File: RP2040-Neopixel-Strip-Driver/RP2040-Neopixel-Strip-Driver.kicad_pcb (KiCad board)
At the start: 4 copper layers, 20.3 x 48.3 mm, 45 parts, among them J201 TYPE-C-31-M-12, J202 Conn_01x03, J203 NeopixelStrip, SW202 ~{USB_BOOT}, U201 AZ1117R-3.3TRE1, U202 RP2040, U205 W25Q128JVS, Y201 Crystal_GND24

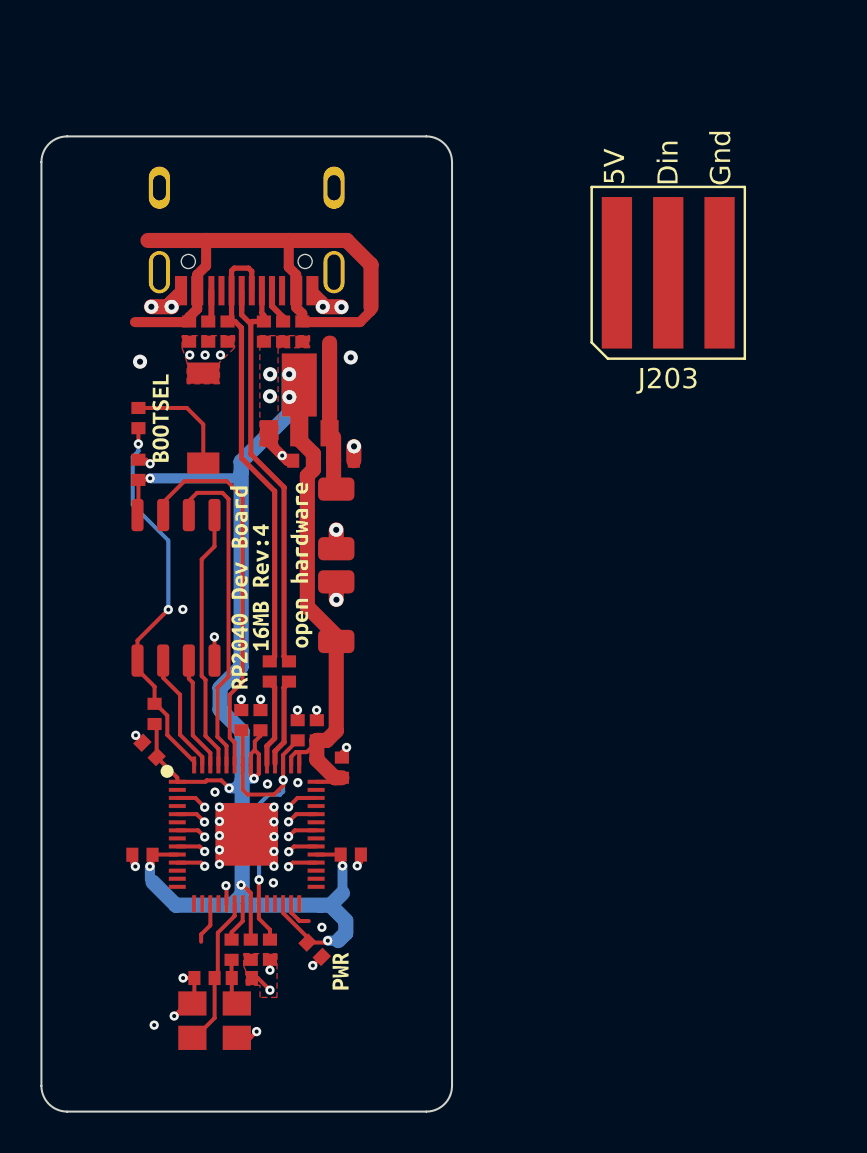
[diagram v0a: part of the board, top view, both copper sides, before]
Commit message: Made new LED strip model and narrowed board.
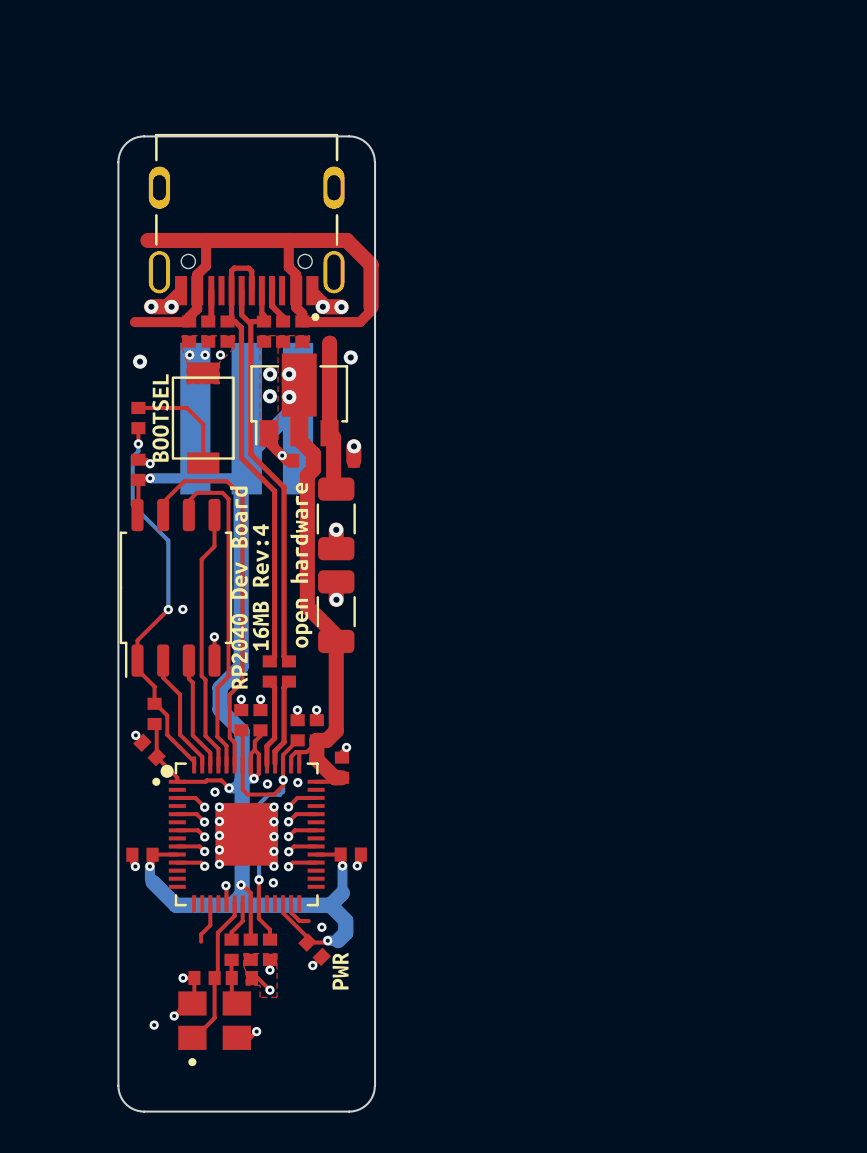
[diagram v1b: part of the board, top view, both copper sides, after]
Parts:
- J203: moved to B.Cu
- moved kibuzzard-62659E4E 59.4 mm to (212.5, 48.8)
- moved kibuzzard-62659F2B 59.4 mm to (200.1, 36.4)
- moved kibuzzard-6265A538 59.4 mm to (206.1, 35.8)
- moved J203 22.1 mm to (146.9, 40.7), turned to 180 degrees
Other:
- board size 20.3 x 48.3 mm -> 12.7 x 48.3 mm

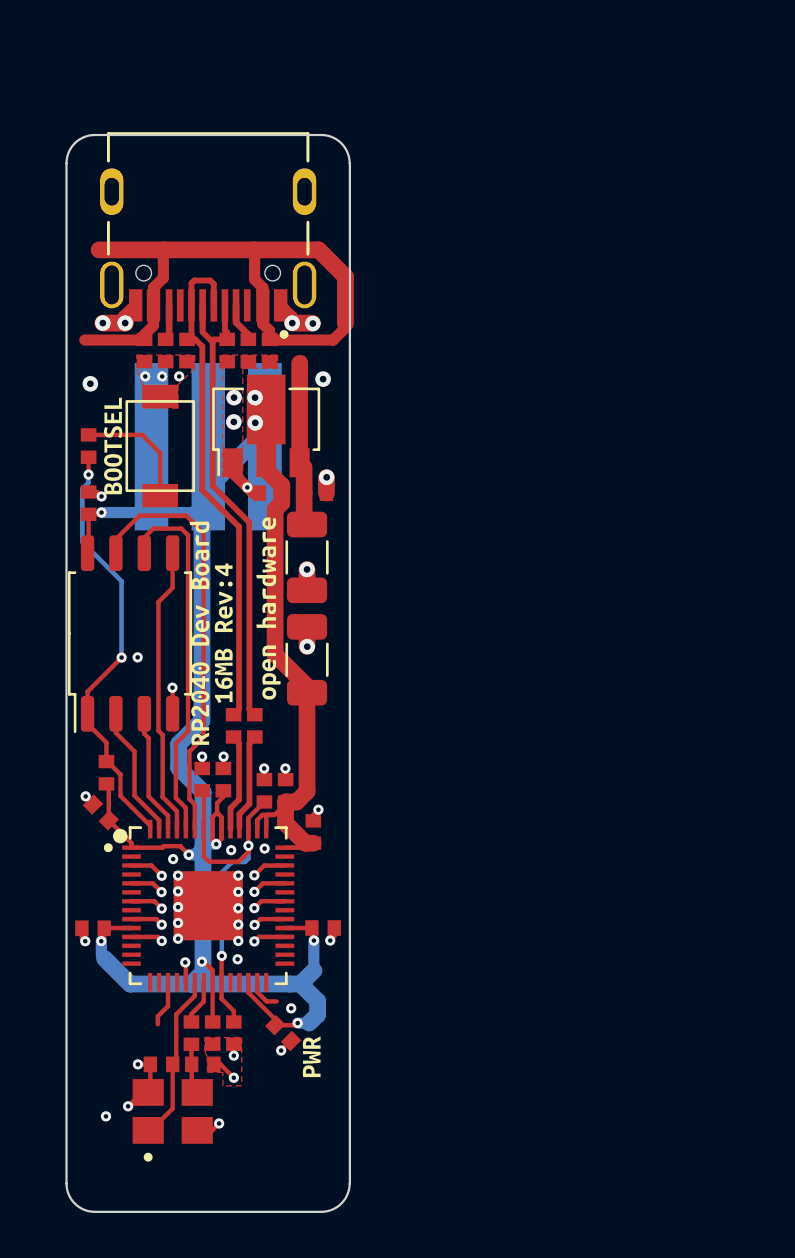
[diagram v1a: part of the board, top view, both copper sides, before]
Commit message: Continued to shrink PCB, replaced regulator and mem with smaller ICs, removed 1206 caps
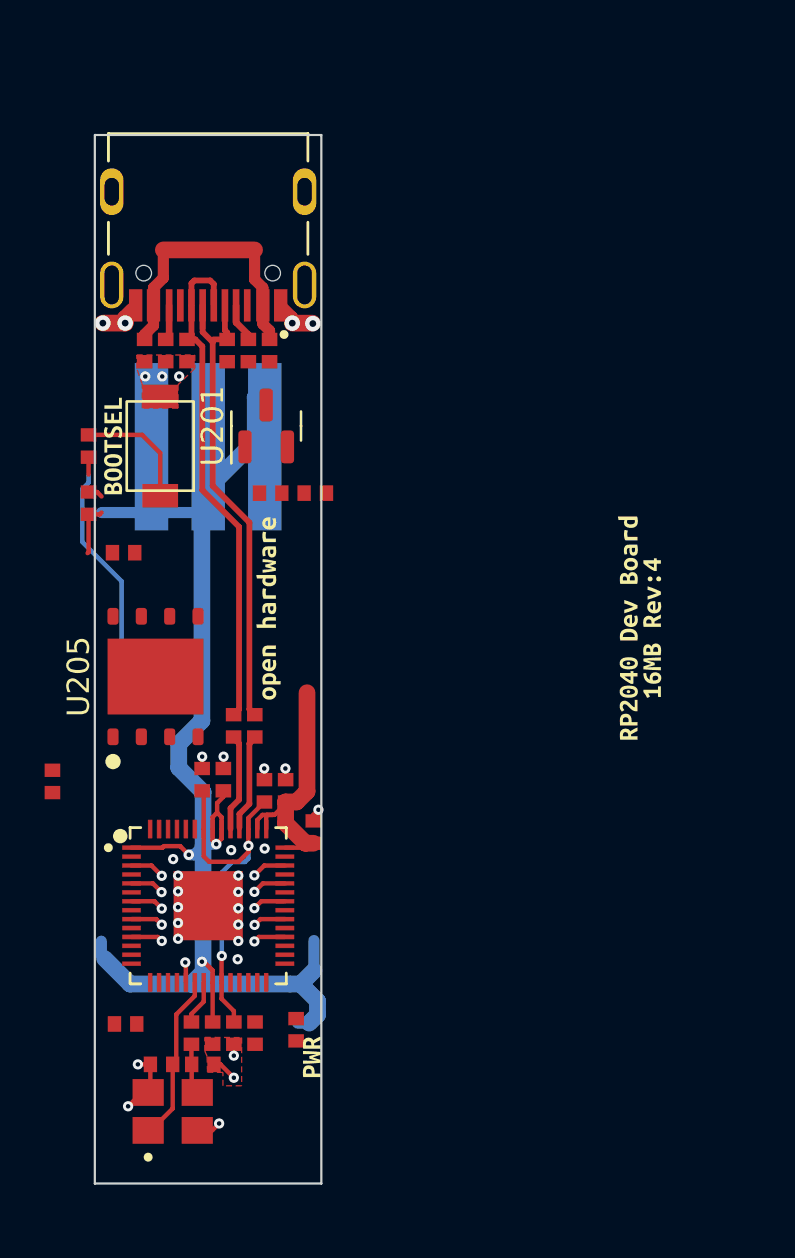
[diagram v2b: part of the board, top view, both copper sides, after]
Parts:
- removed C209, C210: 100uF, Capacitor_SMD:C_1206_3216Metric
- U201: value AZ1117R-3.3TRE1 -> XC6206P332MR; footprint Package_TO_SOT_SMD:SOT-89-3 -> Package_TO_SOT_SMD:SOT-23
- U205: value W25Q128JVS -> W25Q128JVPIQ; footprint Package_SO:SOIC-8_5.23x5.23mm_P1.27mm -> Package_SON:WSON-8-1EP_6x5mm_P1.27mm_EP3.4x4.3mm
- moved kibuzzard-628425F6 19.2 mm to (165.7, 48.9)
- moved kibuzzard-62842605 19.2 mm to (166.8, 48.9)
- moved R213 9.89 mm to (143.1, 45.5), turned to -90 degrees
- moved C213 4.72 mm to (150.8, 66.9), turned to 180 degrees
- moved C215 4.53 mm to (143.2, 66.6), turned to -90 degrees
- moved C212 2.58 mm to (139.9, 55.7), turned to 0 degrees
- moved U205 2.24 mm to (144.6, 51.0)
- moved C221 1.26 mm to (149.0, 67.0), turned to 180 degrees
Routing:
- net 3V3_LDO: track 97.9 -> 74.2 mm, vias 9 -> 3
- net /RP2040/MCU_QSPI_SD3: track 18.9 -> 0.00 mm
- net /RP2040/MCU_QSPI_SCLK: track 16.5 -> 0.00 mm
- net VBUS: track 28.8 -> 12.8 mm
- net /RP2040/MCU_QSPI_SD0: track 13.0 -> 0.00 mm
- net /RP2040/MCU_QSPI_CSN: track 19.3 -> 9.82 mm, vias 2 -> 0
- net GND: track 23.6 -> 14.8 mm, vias 49 -> 32
- net VHI: track 7.50 -> 0.00 mm
- net /RP2040/MCU_QSPI_SD1: track 5.97 -> 0.00 mm
- net /RP2040/MCU_QSPI_SD2: track 5.61 -> 0.00 mm
- net GPIO14: track 2.07 -> 0.00 mm
- net GPIO16: track 1.48 -> 0.00 mm
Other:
- board size 12.7 x 48.3 mm -> 10.2 x 47 mm

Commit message: Update RP2040-Neopixel-Strip-Driver.kicad_pcb
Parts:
- moved kibuzzard-62842635 38.6 mm to (127.6, 37.8)
- moved kibuzzard-62842613 20.0 mm to (169.3, 44.8)
- moved kibuzzard-6284261D 12.9 mm to (130.0, 38.1)
- moved R213 12.0 mm to (131.7, 42.0)
- moved C201 10.5 mm to (162.2, 43.3)
- moved U201 10.3 mm to (150.6, 50.0)
- moved C222 8.27 mm to (134.2, 39.5)
- moved C207 7.37 mm to (157.1, 43.3)
- moved R211 5.42 mm to (136.8, 38.2)
- moved C213 4.11 mm to (151.5, 62.8)
- moved C215 3.90 mm to (142.3, 62.8), turned to 180 degrees
- moved U205 3.10 mm to (144.6, 47.9)
- moved C204 2.64 mm to (151.8, 53.9)
- moved SW202 2.59 mm to (146.9, 39.2), turned to 90 degrees
- moved C208 2.50 mm to (144.9, 53.9)
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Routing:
- net 3V3_LDO: track 74.2 -> 32.4 mm
- net /RP2040/USB_D-: track 22.5 -> 5.05 mm
- net /RP2040/USB_D+: track 22.8 -> 5.49 mm
- net /RP2040/MCU_QSPI_CSN: track 9.82 -> 0.00 mm
- net Net-(R211-Pad1): track 5.46 -> 0.00 mm
- net /RP2040/MCU_USB_D+: track 4.38 -> 0.00 mm
- net /RP2040/MCU_USB_D-: track 4.35 -> 0.00 mm
- net GND: track 14.8 -> 11.4 mm, vias 32 -> 24
- net +1V1: track 16.8 -> 13.5 mm

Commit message: Update RP2040-Neopixel-Strip-Driver.kicad_pcb
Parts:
- moved J203 36.4 mm to (110.6, 38.9)
- moved R211 13.0 mm to (144.4, 48.7), turned to 0 degrees
- moved R213 12.7 mm to (142.7, 48.4), turned to 180 degrees
- moved C212 4.22 mm to (142.3, 59.2), turned to 180 degrees
- moved U205 3.77 mm to (144.6, 44.2)
- moved SW202 1.27 mm to (148.2, 39.2)
- moved C216 1.21 mm to (151.5, 59.2), turned to 180 degrees
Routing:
- net 3V3_LDO: track 32.4 -> 16.4 mm
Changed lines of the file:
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@@
   )
   (footprint "Package_SON:WSON-8-1EP_6x5mm_P1.27mm_EP3.4x4.3mm" (layer "F.Cu")
-    (at 144.565 47.93 90)
+    (at 144.57 44.16 90)
     (descr "WSON, 8 Pin (http://www.winbond.com/resource-files/w25q32jv%20revg%2003272018%20plus.pdf (page 68)), generated with kicad-footprint-generator ipc_noLead_generator.py")
     (tags "WSON NoLead")
@@
   )
   (footprint "Breadstick Footprints:Perfect_0402_Cap" (layer "F.Cu")
-    (at 151.62 58)
+    (at 151.49 59.2 180)
     (property "JLCPCB P/N" "C15525")
     (property "Sheetfile" "RP2040.kicad_sch")
@@
     (fp_line (start -0.85 -1.3) (end 0.85 -1.3) (layer "F.Fab") (width 0.12))
     (fp_line (start -0.85 1.3) (end -0.85 -1.3) (layer "F.Fab") (width 0.12))
-    (pad "1" smd rect (at 0 0.5) (size 0.7 0.6) (layers "F.Cu" "F.Paste" "F.Mask")
+    (pad "1" smd rect (at 0 0.5 180) (size 0.7 0.6) (layers "F.Cu" "F.Paste" "F.Mask")
       (net 53 "3V3_LDO") (pintype "passive"))
-    (pad "2" smd rect (at 0 -0.5) (size 0.7 0.6) (layers "F.Cu" "F.Paste" "F.Mask")
+    (pad "2" smd rect (at 0 -0.5 180) (size 0.7 0.6) (layers "F.Cu" "F.Paste" "F.Mask")
       (net 1 "GND") (pintype "passive"))
     (model "${KICAD6_3DMODEL_DIR}/Capacitor_SMD.3dshapes/C_0402_1005Metric.step"
@@
   )
   (footprint "Breadstick Footprints:Perfect_0402_Resistor" (layer "F.Cu")
-    (at 131.67 42 -90)
+    (at 142.66 48.41 180)
     (property "JLCPCB P/N" "C25744")
     (property "Sheetfile" "RP2040.kicad_sch")
     (property "Sheetname" "RP2040")
     (attr through_hole)
-    (fp_text reference "R213" (at -0.05 1.19) (layer "F.Fab")
+    (fp_text reference "R213" (at -0.05 1.19 90) (layer "F.Fab")
       (effects (font (size 1 1) (thickness 0.15)))
     )
-    (fp_text value "10k" (at 6.8 0.04) (layer "F.Fab")
+    (fp_text value "10k" (at 6.8 0.04 90) (layer "F.Fab")
       (effects (font (size 1 1) (thickness 0.15)))
     )
@@
     (fp_line (start -0.85 -1.3) (end 0.85 -1.3) (layer "F.Fab") (width 0.12))
     (fp_line (start 0.85 -1.3) (end 0.85 1.3) (layer "F.Fab") (width 0.12))
-    (pad "1" smd rect (at 0 0.5 270) (size 0.7 0.6) (layers "F.Cu" "F.Paste" "F.Mask")
+    (pad "1" smd rect (at 0 0.5 180) (size 0.7 0.6) (layers "F.Cu" "F.Paste" "F.Mask")
       (net 16 "/RP2040/MCU_QSPI_CSN") (pintype "passive"))
-    (pad "2" smd rect (at 0 -0.5 270) (size 0.7 0.6) (layers "F.Cu" "F.Paste" "F.Mask")
+    (pad "2" smd rect (at 0 -0.5 180) (size 0.7 0.6) (layers "F.Cu" "F.Paste" "F.Mask")
       (net 53 "3V3_LDO") (pintype "passive"))
     (model "${KICAD6_3DMODEL_DIR}/Resistor_SMD.3dshapes/R_0402_1005Metric.step"
@@
   )
   (footprint "Breadstick Footprints:GT-TC029B-H025-L1N" (layer "F.Cu")
-    (at 146.91 39.25 90)
+    (at 148.175 39.25 90)
     (property "JLCPCB P/N" "C843669")
     (property "Sheetfile" "RP2040.kicad_sch")
@@
   )
   (footprint "Breadstick Footprints:Perfect_0402_Resistor" (layer "F.Cu")
-    (at 136.75 38.19 180)
+    (at 144.44 48.68)
     (property "JLCPCB P/N" "C11702")
     (property "Sheetfile" "RP2040.kicad_sch")
@@
     (fp_line (start -0.85 -1.3) (end 0.85 -1.3) (layer "F.Fab") (width 0.12))
     (fp_line (start 0.85 -1.3) (end 0.85 1.3) (layer "F.Fab") (width 0.12))
-    (pad "1" smd rect (at 0 0.5 180) (size 0.7 0.6) (layers "F.Cu" "F.Paste" "F.Mask")
+    (pad "1" smd rect (at 0 0.5) (size 0.7 0.6) (layers "F.Cu" "F.Paste" "F.Mask")
       (net 15 "Net-(R211-Pad1)") (pintype "passive"))
-    (pad "2" smd rect (at 0 -0.5 180) (size 0.7 0.6) (layers "F.Cu" "F.Paste" "F.Mask")
+    (pad "2" smd rect (at 0 -0.5) (size 0.7 0.6) (layers "F.Cu" "F.Paste" "F.Mask")
       (net 16 "/RP2040/MCU_QSPI_CSN") (pintype "passive"))
     (model "${KICAD6_3DMODEL_DIR}/Resistor_SMD.3dshapes/R_0402_1005Metric.step"
@@
   )
   (footprint "Breadstick Footprints:Perfect_0402_Cap" (layer "F.Cu")
-    (at 139.93 55.73)
+    (at 142.33 59.2 180)
     (property "JLCPCB P/N" "C15525")
     (property "Sheetfile" "RP2040.kicad_sch")
@@
     (fp_line (start -0.85 -1.3) (end 0.85 -1.3) (layer "F.Fab") (width 0.12))
     (fp_line (start -0.85 1.3) (end -0.85 -1.3) (layer "F.Fab") (width 0.12))
-    (pad "1" smd rect (at 0 0.5) (size 0.7 0.6) (layers "F.Cu" "F.Paste" "F.Mask")
+    (pad "1" smd rect (at 0 0.5 180) (size 0.7 0.6) (layers "F.Cu" "F.Paste" "F.Mask")
       (net 53 "3V3_LDO") (pintype "passive"))
-    (pad "2" smd rect (at 0 -0.5) (size 0.7 0.6) (layers "F.Cu" "F.Paste" "F.Mask")
+    (pad "2" smd rect (at 0 -0.5 180) (size 0.7 0.6) (layers "F.Cu" "F.Paste" "F.Mask")
       (net 1 "GND") (pintype "passive"))
     (model "${KICAD6_3DMODEL_DIR}/Capacitor_SMD.3dshapes/C_0402_1005Metric.step"
@@
   )
   (footprint "Breadstick Footprints:NeopixelStrip" (layer "B.Cu")
-    (at 146.91 40.73 180)
+    (at 110.58 38.9 180)
     (property "Sheetfile" "RP2040.kicad_sch")
     (property "Sheetname" "RP2040")
@@
   (segment (start 147.31 56.7) (end 147.31 57.13) (width 0.2) (layer "F.Cu") (net 53))
   (segment (start 146.72 63.81) (end 146.63 63.81) (width 0.2) (layer "F.Cu") (net 53))
-  (segment (start 151.42 58.7) (end 151.62 58.5) (width 0.2) (layer "F.Cu") (net 53))
   (segment (start 147.11 57.865) (end 147.11 57.33) (width 0.2) (layer "F.Cu") (net 53))
   (segment (start 146.99 64.08) (end 146.72 63.81) (width 0.2) (layer "F.Cu") (net 53))
@@
   (via (at 146.63 63.81) (size 0.46) (drill 0.2) (layers "F.Cu" "B.Cu") (net 53))
   (via (at 147.27 58.54) (size 0.46) (drill 0.2) (layers "F.Cu" "B.Cu") (net 53))
-  (segment (start 142.12 62.89) (end 142.12 63.52) (width 0.5) (layer "B.Cu") (net 53))
-  (segment (start 143.41 64.81) (end 142.27 63.67) (width 0.75) (layer "B.Cu") (net 53))
-  (segment (start 150.58 64.81) (end 146.15 64.81) (width 0.75) (layer "B.Cu") (net 53))
-  (segment (start 146.15 64.81) (end 146.68 64.28) (width 0.75) (layer "B.Cu") (net 53))
   (segment (start 147.27 58.54) (end 146.76 58.54) (width 0.5) (layer "B.Cu") (net 53))
-  (segment (start 151.65 64.21) (end 151.05 64.81) (width 0.75) (layer "B.Cu") (net 53))
   (segment (start 146.68 58.62) (end 146.68 61.98) (width 0.75) (layer "B.Cu") (net 53))
-  (segment (start 151.05 64.81) (end 151.81 65.57) (width 0.75) (layer "B.Cu") (net 53))
   (segment (start 146.042396 59.017918) (end 146.282082 59.017918) (width 0.5) (layer "B.Cu") (net 53))
-  (segment (start 151.65 62.86) (end 151.65 64.21) (width 0.5) (layer "B.Cu") (net 53))
-  (segment (start 150.921879 66.560751) (end 151.439249 66.560751) (width 0.5) (layer "B.Cu") (net 53))
   (segment (start 146.68 64.28) (end 146.68 61.98) (width 0.75) (layer "B.Cu") (net 53))
   (segment (start 146.282082 59.017918) (end 146.68 58.62) (width 0.5) (layer "B.Cu") (net 53))
   (segment (start 146.76 58.54) (end 146.68 58.62) (width 0.2) (layer "B.Cu") (net 53))
-  (segment (start 143.41 64.81) (end 146.15 64.81) (width 0.75) (layer "B.Cu") (net 53))
-  (segment (start 150.58 64.81) (end 151.05 64.81) (width 0.75) (layer "B.Cu") (net 53))
-  (segment (start 142.12 63.52) (end 142.27 63.67) (width 0.2) (layer "B.Cu") (net 53))
-  (segment (start 151.81 66.19) (end 151.81 65.57) (width 0.75) (layer "B.Cu") (net 53))
-  (segment (start 151.439249 66.560751) (end 151.81 66.19) (width 0.75) (layer "B.Cu") (net 53))
   (segment (start 144.06 35.7) (end 144.46 35.3) (width 0.5) (layer "F.Cu") (net 57))
   (segment (start 149.66 35.53) (end 149.36 35.23) (width 0.5) (layer "F.Cu") (net 57))
